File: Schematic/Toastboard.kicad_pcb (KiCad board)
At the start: 2 copper layers, 70 x 55 mm, 46 parts, among them J1 Conn_01x20_Female, J2 USB_B_Micro, Q1 FDS6892A, SW5 SW_DIP_x04, U1 24LC01, U2 PCT2075D, U3 AMS1117-3.3

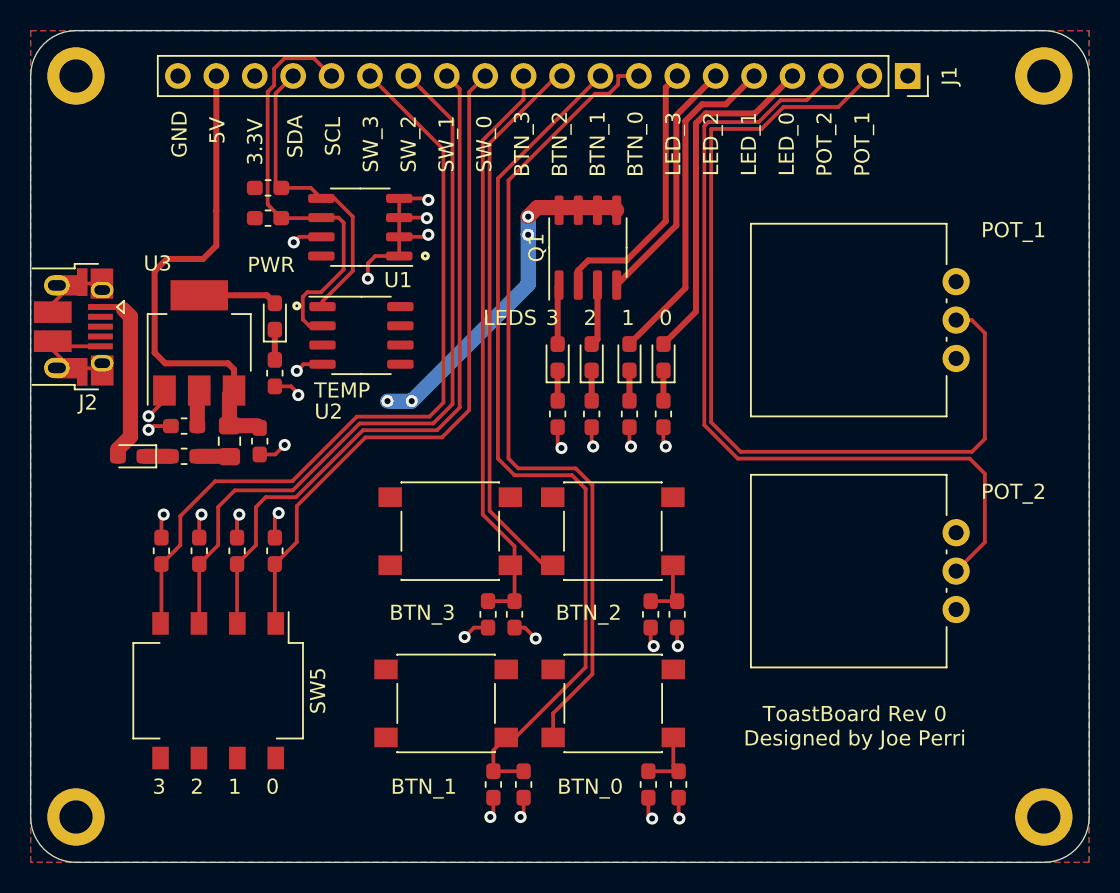
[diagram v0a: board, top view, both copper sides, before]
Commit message: Increased via size. Added JLC tracking number
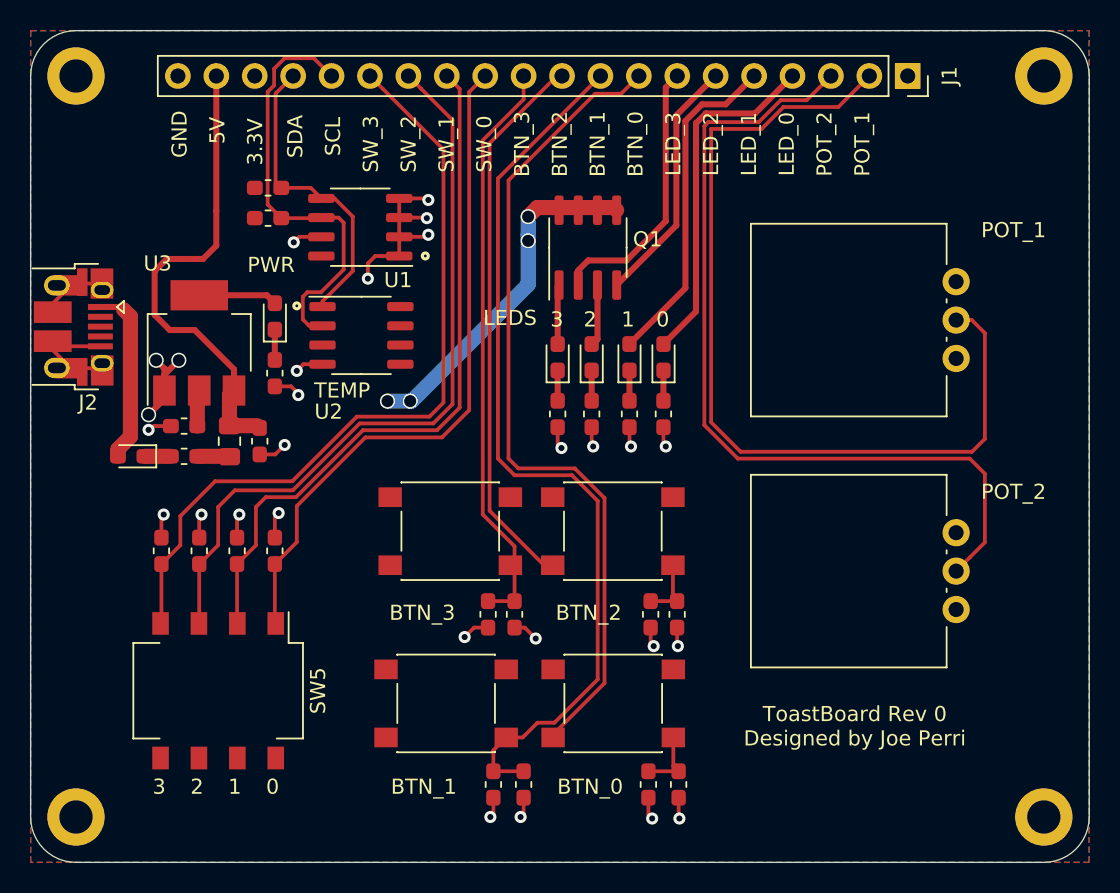
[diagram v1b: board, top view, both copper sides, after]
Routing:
- net GND: track 59.7 -> 64.8 mm, vias 26 -> 28
- net /BTN_1: track 58.3 -> 59.9 mm
- net +5V: track 33.0 -> 31.5 mm
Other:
- board text added: "JLCJLCJLCJLC"

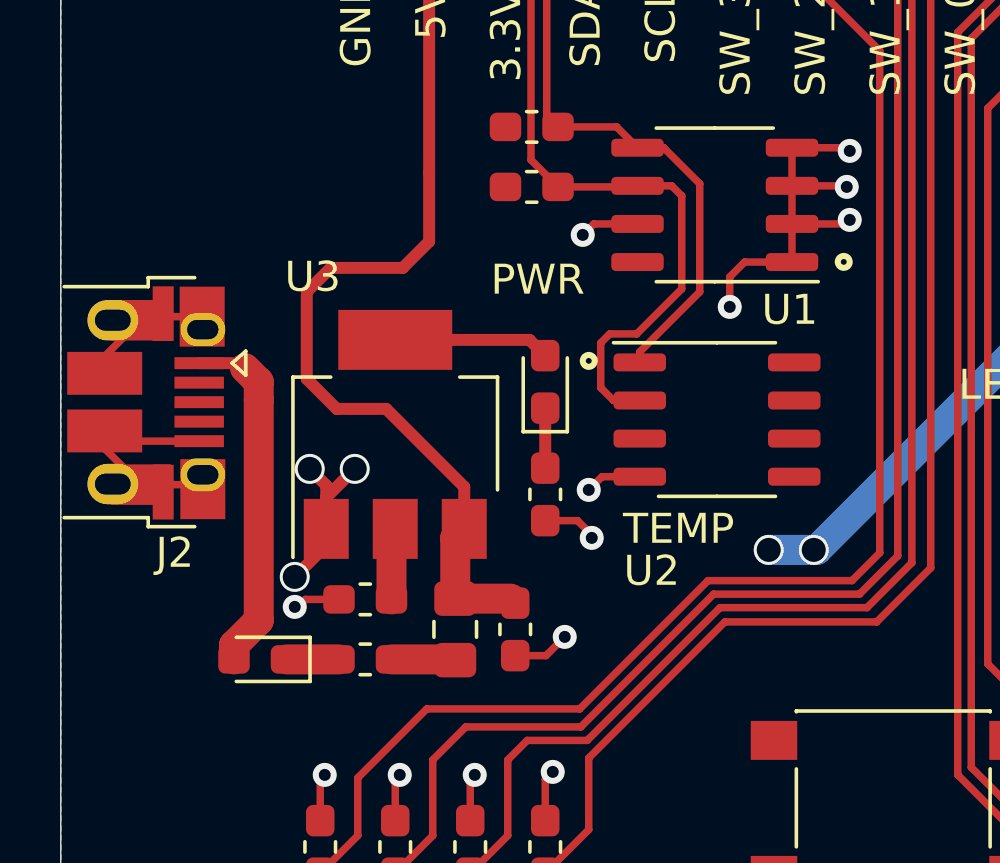
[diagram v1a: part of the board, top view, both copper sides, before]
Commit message: Change footprints to match available parts
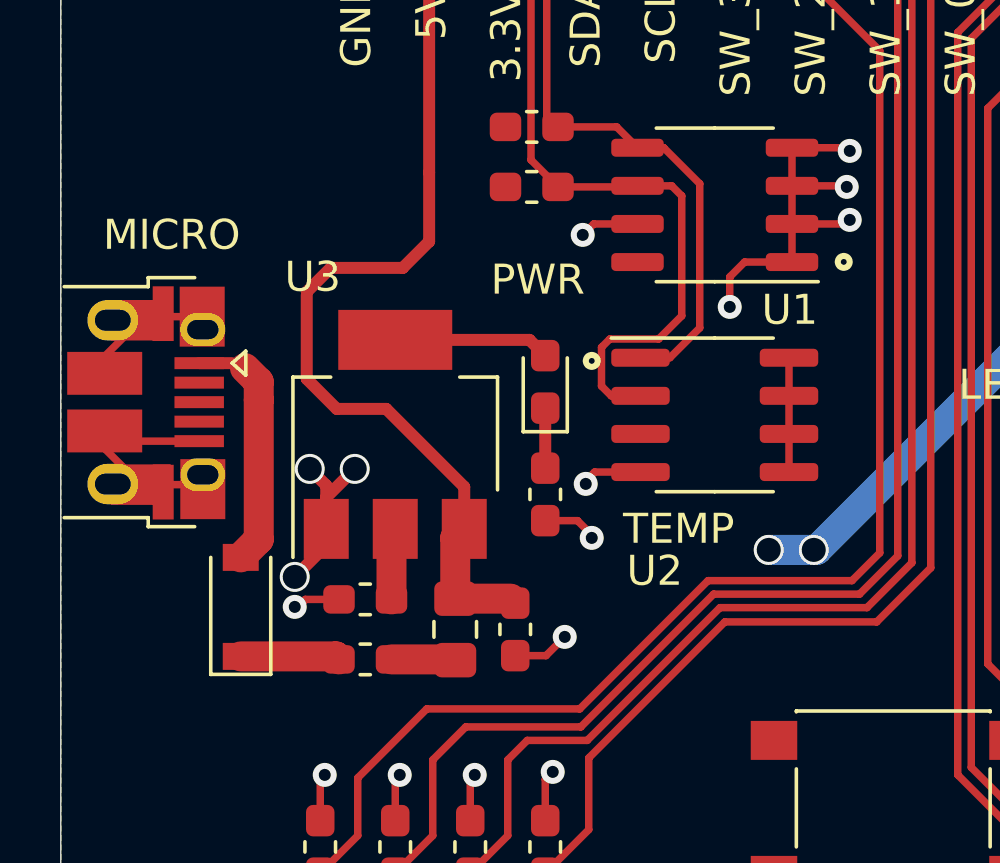
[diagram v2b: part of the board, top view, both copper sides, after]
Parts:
- D2: footprint Diode_SMD:D_0603_1608Metric_Pad1.05x0.95mm_HandSolder -> Diode_SMD:D_SOD-123
- U2: value PCT2075D -> LM75B; footprint Package_SO:SO-8_3.9x4.9mm_P1.27mm -> Package_SO:SOIC-8_3.9x4.9mm_P1.27mm
- moved D2 1.87 mm to (66.0, 72.4), turned to 90 degrees
- moved U2 0.17 mm to (81.8, 66.0)
- renumbered J2 to MICRO
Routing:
- net +3V3: track 30.9 -> 34.7 mm
- net Net-(D2-Pad2): track 11.7 -> 8.18 mm
- net Net-(D2-Pad1): track 1.75 -> 3.32 mm
